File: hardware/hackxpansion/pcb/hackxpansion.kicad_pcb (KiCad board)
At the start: 4 copper layers, 52 x 69 mm, 97 parts, among them CN1 533981471, CN2 533981471, CN3 533981471, CN4 533981471, IC1 ADS7128IRTET, J1 Conn_01x03_MountingPin, J2 USB_C_Receptacle_USB2.0_14P, Q1 BSS138, Q2 2N7002, SW1 SW_Push, SW2 SW_Push, SW3 SW_On_Off, U2 RP2354B, U5 SPX3819M5-L-3-3, U7 BQ24075RGT, U8 USBLC6-2SC6, Y1 ABM8-272-T3

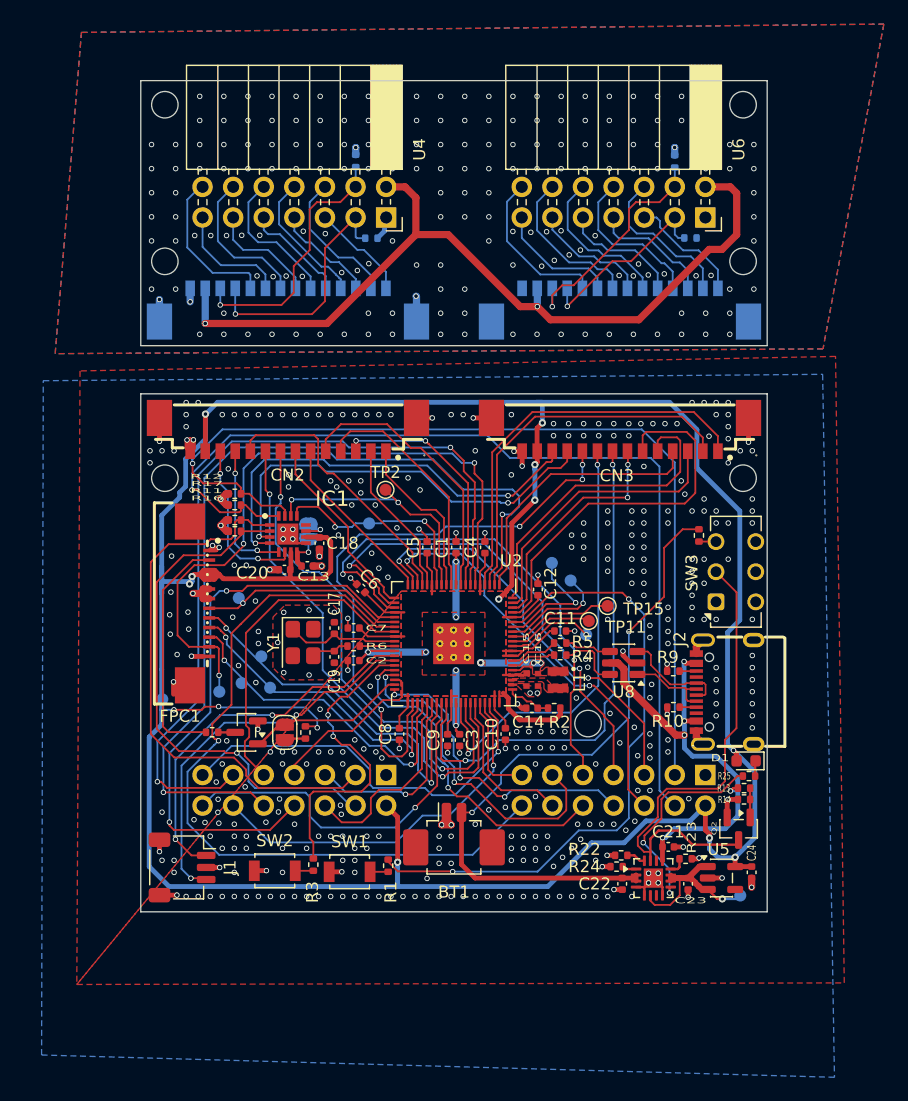
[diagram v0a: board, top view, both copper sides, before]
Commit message: added series resistor to module power rail, so it can now do hotswap
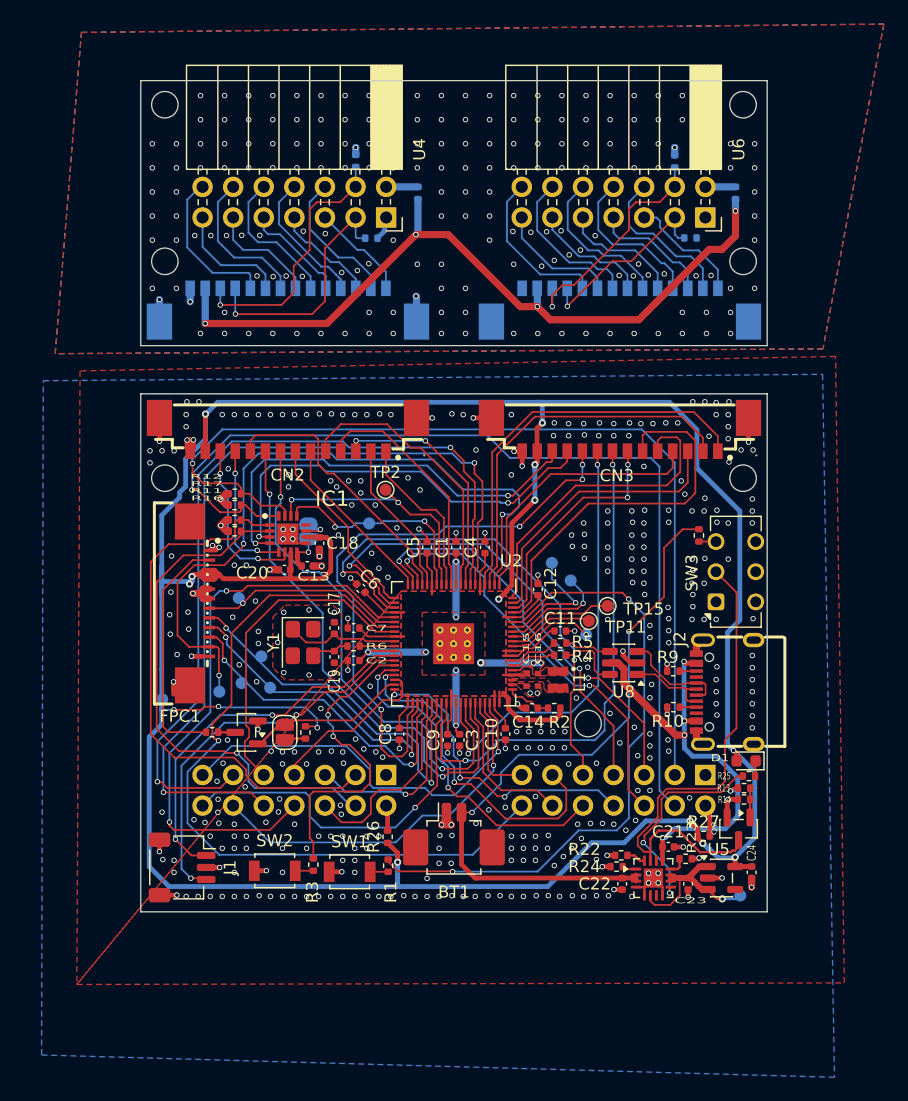
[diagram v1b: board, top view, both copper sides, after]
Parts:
- added R26: 5R, Resistor_SMD:R_0402_1005Metric, F.Cu at (122.4, 94.7)
- added R27: 5R, Resistor_SMD:R_0402_1005Metric, F.Cu at (148.6, 94.6)
- added R28: 5R, Resistor_SMD:R_0402_1005Metric, B.Cu at (124.9, 41.2)
- added R29: 5R, Resistor_SMD:R_0402_1005Metric, B.Cu at (151.2, 41.2)
- R11, R12, R16, R17, R18, R19, R20, R21: value 10K -> 10k
- R7: value 10 -> 10R
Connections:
- U1 pad 2: /+3V3 -> Net-(U1-3V3)
- U3 pad 2: /+3V3 -> Net-(U3-3V3)
- U4 pad 2: /DAUGHT_+3V3 -> Net-(U4-3V3)
- U6 pad 2: /DAUGHT_+3V3 -> Net-(U6-3V3)
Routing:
- net /DAUGHT_+3V3: track 69.6 -> 63.4 mm, vias 2 -> 4
- net /+3V3: track 300.5 -> 294.9 mm, vias 14 -> 15
- net Net-(U3-3V3): track 0.00 -> 2.67 mm
- net Net-(U4-3V3): track 0.00 -> 2.64 mm
- net Net-(U6-3V3): track 0.00 -> 2.50 mm
- net Net-(U1-3V3): track 0.00 -> 2.13 mm
- net /Main Board/Power/SYSOFF: track 40.7 -> 41.2 mm

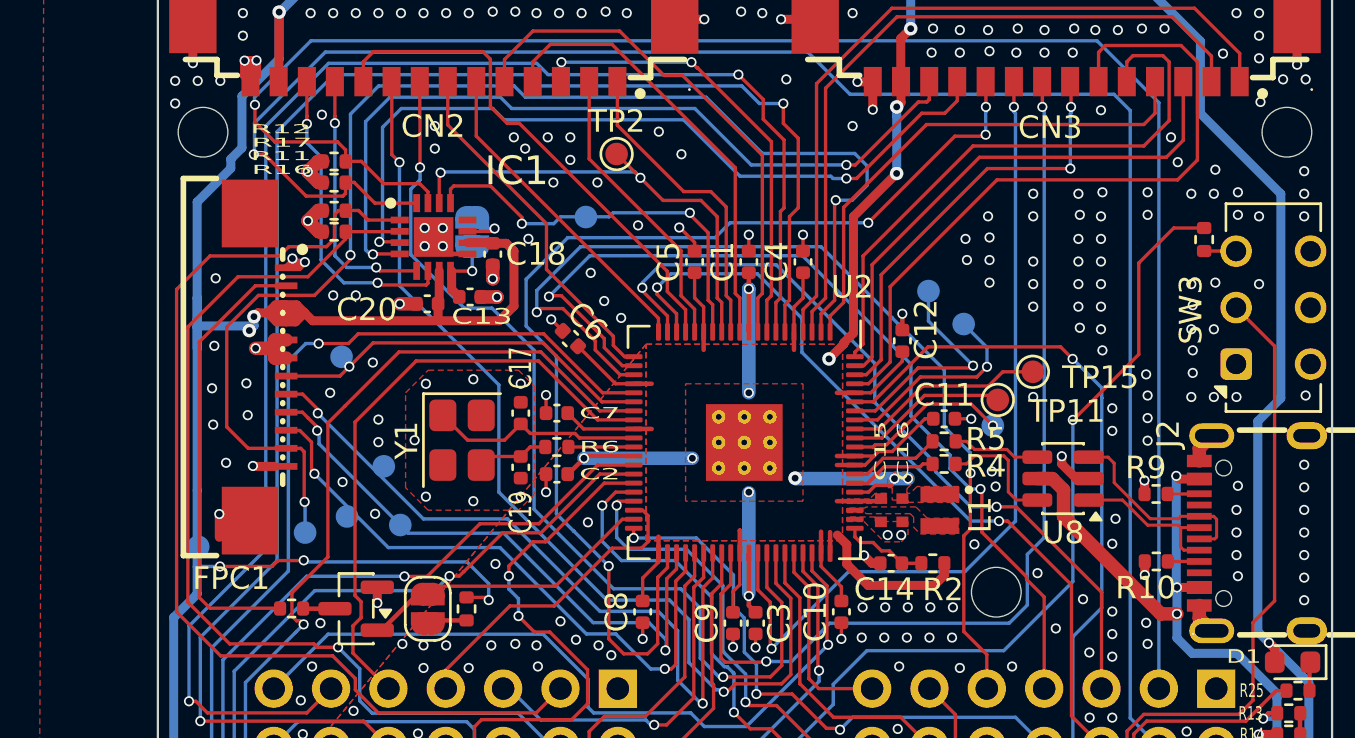
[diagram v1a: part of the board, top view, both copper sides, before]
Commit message: changed out fpc connector, fixed usb dp width
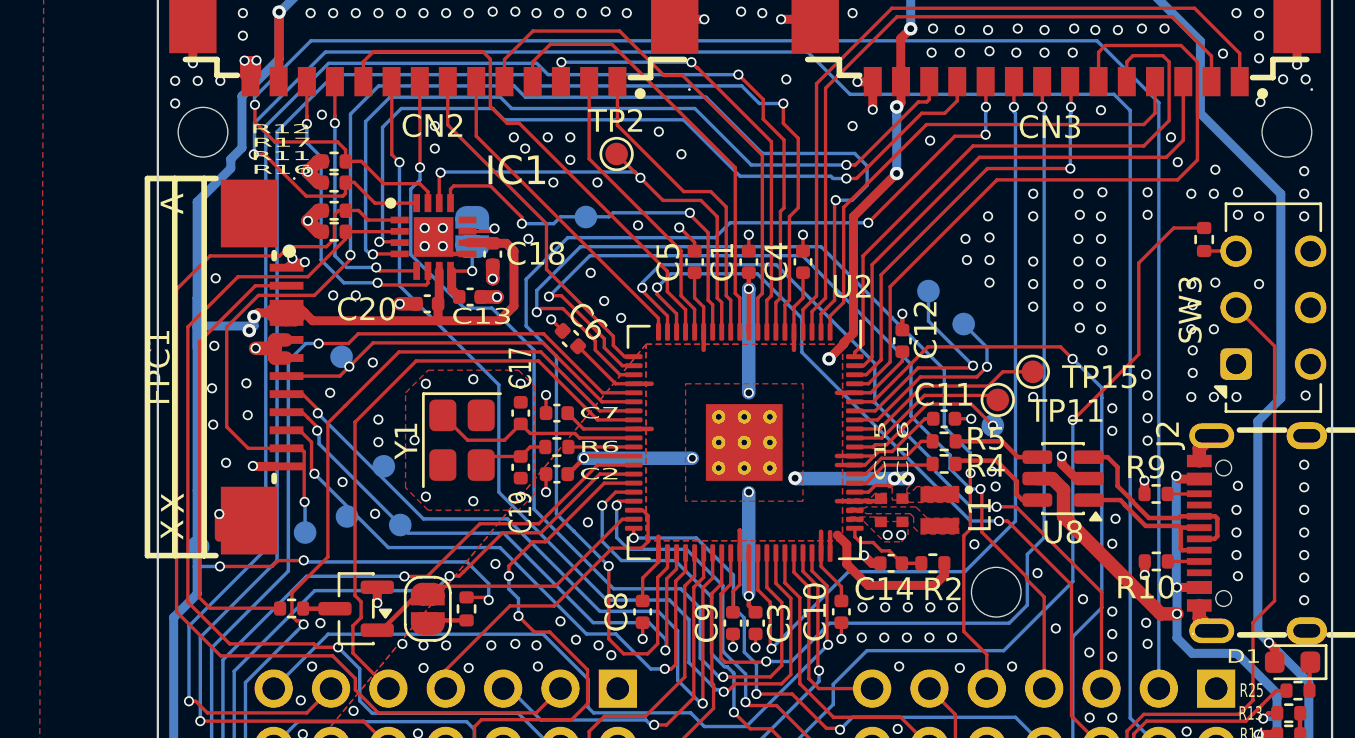
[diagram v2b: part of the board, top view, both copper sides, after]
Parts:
- FPC1: footprint easyeda2kicad:FPC-SMD_AFC08-S12ECA-00 -> easyeda2kicad:FPC-SMD_P0.80-12P_LCS-SJ-H2.0
- turned FPC1 to 90 degrees
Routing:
- net /Main Board/Display/RESET: track 58.8 -> 59.8 mm
- net /GND: track 63.5 -> 62.5 mm, vias 381 -> 382
- net /Main Board/RP2354B/D-: track 5.40 -> 4.74 mm

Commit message: fixed issues with new fpc
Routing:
- net /GND: track 62.5 -> 64.4 mm
- net /Main Board/Display/RESET: track 59.8 -> 61.0 mm
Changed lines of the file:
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@@
 		(capping no)
 		(filling no)
-		(zone_defaults)
 		(grid_origin 122.239998 40.72)
 		(pcbplotparams
@@
 	)
 	(segment
+		(start 105.62 81.81)
+		(end 105.91 82.1)
+		(width 0.4)
+		(layer "F.Cu")
+		(net "/GND")
+	)
+	(segment
 		(start 147.610459 96.500266)
 		(end 148.149423 96.500266)
@@
 	)
 	(segment
+		(start 104.59 81.81)
+		(end 105.62 81.81)
+		(width 0.4)
+		(layer "F.Cu")
+		(net "/GND")
+	)
+	(segment
 		(start 114.83 70.29)
 		(end 114.08 69.54)
@@
 	)
 	(segment
-		(start 104.59 82.840001)
-		(end 104.59 81.81)
-		(width 0.4)
-		(layer "F.Cu")
-		(net "/GND")
-	)
-	(segment
 		(start 107.827121 70.622879)
 		(end 107.55 70.9)
@@
 	)
 	(segment
+		(start 107.57 79.7)
+		(end 106.069998 79.7)
+		(width 0.4)
+		(layer "F.Cu")
+		(net "/GND")
+	)
+	(segment
 		(start 127.244998 93.277787)
 		(end 127.244998 92.65)
@@
 	)
 	(via
+		(at 106.069998 79.7)
+		(size 0.45)
+		(drill 0.3)
+		(layers "F.Cu" "B.Cu")
+		(net "/GND")
+	)
+	(via
 		(at 136.2 97.06)
 		(size 0.45)
@@
 	)
 	(via
-		(at 106.08 79.68)
-		(size 0.45)
-		(drill 0.3)
-		(layers "F.Cu" "B.Cu")
-		(free yes)
-		(net "/GND")
-	)
-	(via
 		(at 103.635738 92.625706)
 		(size 0.45)
@@
 	)
 	(segment
-		(start 108.676572 79.89654)
-		(end 108.676572 78.626572)
-		(width 0.15)
-		(layer "F.Cu")
-		(net "/Main Board/Display/MOSI")
-	)
-	(segment
 		(start 124.32 88.668245)
 		(end 124.61 88.668245)
@@
 	)
 	(segment
-		(start 108.676572 78.626572)
+		(start 108.829998 78.779998)
 		(end 108.16 78.11)
 		(width 0.15)
@@
 	)
 	(segment
-		(start 107.559999 78.11)
-		(end 107.549999 78.1)
+		(start 108.829998 79.519995)
+		(end 108.829998 78.779998)
 		(width 0.15)
 		(layer "F.Cu")
@@
 	)
 	(segment
+		(start 107.559999 78.11)
+		(end 107.549999 78.1)
+		(width 0.15)
+		(layer "F.Cu")
+		(net "/Main Board/Display/MOSI")
+	)
+	(segment
 		(start 108.16 78.11)
 		(end 107.559999 78.11)
@@
 	)
 	(segment
-		(start 108.805016 80.024984)
-		(end 108.676572 79.89654)
+		(start 108.950003 79.64)
+		(end 108.829998 79.519995)
 		(width 0.15)
 		(layer "F.Cu")
@@
 	)
 	(via
-		(at 108.805016 80.024984)
+		(at 108.950003 79.64)
 		(size 0.45)
 		(drill 0.3)
@@
 	)
 	(segment
-		(start 120.85 87.12)
-		(end 122.15 87.12)
+		(start 122.15 87.12)
+		(end 123.698245 88.668245)
 		(width 0.15)
 		(layer "B.Cu")
@@
 	)
 	(segment
-		(start 112.075032 83.295)
-		(end 117.025 83.295)
+		(start 108.950003 80.169971)
+		(end 112.075032 83.295)
 		(width 0.15)
 		(layer "B.Cu")
@@
 	)
 	(segment
-		(start 122.15 87.12)
-		(end 123.698245 88.668245)
+		(start 108.950003 79.64)
+		(end 108.950003 80.169971)
 		(width 0.15)
 		(layer "B.Cu")
@@
 	)
 	(segment
-		(start 108.805016 80.024984)
-		(end 112.075032 83.295)
+		(start 120.85 87.12)
+		(end 122.15 87.12)
+		(width 0.15)
+		(layer "B.Cu")
+		(net "/Main Board/Display/MOSI")
+	)
+	(segment
+		(start 120.15 86.373603)
+		(end 120.15 86.42)
 		(width 0.15)
 		(layer "B.Cu")
@@
 	)
 	(segment
+		(start 119.886397 86.11)
+		(end 120.15 86.373603)
+		(width 0.15)
+		(layer "B.Cu")
+		(net "/Main Board/Display/MOSI")
+	)
+	(segment
 		(start 117.025 83.295)
+		(end 119.84 86.11)
+		(width 0.15)
+		(layer "B.Cu")
+		(net "/Main Board/Display/MOSI")
+	)
+	(segment
+		(start 119.84 86.11)
+		(end 119.886397 86.11)
+		(width 0.15)
+		(layer "B.Cu")
+		(net "/Main Board/Display/MOSI")
+	)
+	(segment
+		(start 120.15 86.42)
 		(end 120.85 87.12)
 		(width 0.15)
@@
 	)
 	(segment
-		(start 110.4 70.53)
-		(end 108.805 72.125)
+		(start 112.075032 83.295)
+		(end 117.025 83.295)
+		(width 0.15)
+		(layer "B.Cu")
+		(net "/Main Board/Display/MOSI")
+	)
+	(segment
+		(start 104.921117 77.951117)
+		(end 105.87 78.9)
 		(width 0.15)
 		(layer "F.Cu")
@@
 	)
 	(segment
-		(start 108.805 72.125)
-		(end 106.324999 72.125)
+		(start 107.37 80.27)
+		(end 105.809998 80.27)
 		(width 0.15)
 		(layer "F.Cu")
@@
 	)
 	(segment
-		(start 107.05 79.7)
-		(end 106.1 79.7)
-		(width 0.4)
+		(start 105.509998 79.97)
+		(end 105.509998 79.260002)
+		(width 0.15)
 		(layer "F.Cu")
 		(net "/Main Board/Display/RESET")
 	)
 	(segment
-		(start 131.890003 67.91)
-		(end 131.840001 67.960002)
+		(start 108.83 72.1)
+		(end 106.349999 72.1)
 		(width 0.15)
 		(layer "F.Cu")
@@
 	)
 	(segment
-		(start 105.87 78.9)
-		(end 107.05 78.9)
+		(start 105.509998 79.260002)
+		(end 105.87 78.9)
 		(width 0.15)
 		(layer "F.Cu")
@@
 	)
 	(segment
-		(start 131.840001 67.960002)
-		(end 131.840001 72.34)
+		(start 110.4 70.34)
+		(end 110.4 70.53)
 		(width 0.15)
 		(layer "F.Cu")
@@
 	)
 	(segment
-		(start 108.35 81.25)
-		(end 108.35 79.05)
+		(start 131.890003 67.91)
+		(end 131.840001 67.960002)
 		(width 0.15)
 		(layer "F.Cu")
@@
 	)
 	(segment
-		(start 104.921117 73.528882)
-		(end 104.921117 77.951117)
+		(start 105.87 78.9)
+		(end 107.05 78.9)
 		(width 0.15)
 		(layer "F.Cu")
@@
 	)
 	(segment
-		(start 108.35 79.05)
-		(end 108.2 78.9)
+		(start 131.840001 67.960002)
+		(end 131.840001 72.34)
 		(width 0.15)
 		(layer "F.Cu")
@@
 	)
 	(segment
-		(start 106.324999 72.125)
-		(end 104.921117 73.528882)
+		(start 105.809998 80.27)
+		(end 105.509998 79.97)
 		(width 0.15)
 		(layer "F.Cu")
@@
 	)
 	(segment
-		(start 131.840001 72.34)
-		(end 131.240001 72.94)
+		(start 106.349999 72.1)
+		(end 104.921117 73.528882)
 		(width 0.15)
 		(layer "F.Cu")
@@
 	)
 	(segment
-		(start 106.1 79.7)
-		(end 106.08 79.68)
+		(start 131.840001 72.34)
+		(end 131.240001 72.94)
 		(width 0.15)
 		(layer "F.Cu")
@@
 	)
 	(segment
-		(start 104.921117 77.951117)
-		(end 105.87 78.9)
+		(start 110.4 70.53)
+		(end 108.83 72.1)
 		(width 0.15)
 		(layer "F.Cu")
@@
 	)
 	(segment
-		(start 131.240001 72.94)
-		(end 131.240002 73.743499)
+		(start 108.37 81.27)
+		(end 107.37 80.27)
 		(width 0.15)
 		(layer "F.Cu")
@@
 	)
 	(segment
-		(start 107.8 78.9)
-		(end 107.05 78.9)
+		(start 104.921117 73.528882)
+		(end 104.921117 77.951117)
 		(width 0.15)
 		(layer "F.Cu")
@@
 	)
 	(segment
-		(start 108.37 81.27)
-		(end 108.35 81.25)
+		(start 131.240001 72.94)
+		(end 131.240002 73.743499)
 		(width 0.15)
 		(layer "F.Cu")
@@
 	)
 	(segment
-		(start 110.4 70.34)
-		(end 110.4 70.53)
+		(start 107.8 78.9)
+		(end 107.05 78.9)
 		(width 0.15)
 		(layer "F.Cu")
@@
 	)
 	(segment
-		(start 108.511644 71.301644)
-		(end 110.18677 69.626519)
+		(start 105.42 71.3)
+		(end 108.513289 71.3)
 		(width 0.15)
 		(layer "F.Cu")
@@
 	)
 	(segment
-		(start 103.2 85.710001)
-		(end 103.2 73.52)
+		(start 108.93 87.710001)
+		(end 108.78 87.560001)
 		(width 0.15)
 		(layer "F.Cu")
@@
 	)
 	(segment
-		(start 110.185591 69.304687)
-		(end 112.565313 69.304687)
+		(start 108.78 87.560001)
+		(end 105.05 87.560001)
 		(width 0.15)
 		(layer "F.Cu")
@@
 	)
 	(segment
-		(start 105.05 87.560001)
-		(end 103.2 85.710001)
+		(start 110.185591 69.304687)
+		(end 112.565313 69.304687)
 		(width 0.15)
 		(layer "F.Cu")
@@
 	)
 	(segment
-		(start 105.418356 71.301644)
-		(end 108.511644 71.301644)
+		(start 103.2 73.52)
+		(end 105.42 71.3)
 		(width 0.15)
 		(layer "F.Cu")
@@
 	)
 	(segment
-		(start 108.93 87.710001)
-		(end 108.78 87.560001)
+		(start 105.05 87.560001)
+		(end 103.2 85.710001)
 		(width 0.15)
 		(layer "F.Cu")
@@
 	)
 	(segment
-		(start 108.78 87.560001)
-		(end 105.05 87.560001)
+		(start 109.851316 87.71)
+		(end 109.851315 87.710001)
 		(width 0.15)
 		(layer "F.Cu")
@@
 	)
 	(segment
-		(start 109.851316 87.71)
-		(end 109.851315 87.710001)
+		(start 109.851315 87.710001)
+		(end 108.93 87.710001)
 		(width 0.15)
 		(layer "F.Cu")
@@
 	)
 	(segment
-		(start 103.2 73.52)
-		(end 105.418356 71.301644)
+		(start 103.2 85.710001)
+		(end 103.2 73.52)
 		(width 0.15)
 		(layer "F.Cu")
@@
 	)
 	(segment
-		(start 109.851315 87.710001)
-		(end 108.93 87.710001)
+		(start 108.513289 71.3)
+		(end 110.18677 69.626519)
 		(width 0.15)
 		(layer "F.Cu")
